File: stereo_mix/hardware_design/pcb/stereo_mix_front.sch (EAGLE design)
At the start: 31 parts, among them U1 THONKICONNOLD, U10 THONKICONNOLD, U11 THONKICONNOLD, U12 THONKICONNOLD, U13 THONKICONNOLD, U14 THONKICONNOLD, U15 THONKICONNOLD, U16 THONKICONNOLD, U17 THONKICONNOLD, U18 THONKICONNOLD, U19 THONKICONNOLD, U2 THONKICONNOLD, U20 THONKICONNOLD, U3 THONKICONNOLD, U4 THONKICONNOLD, U5 THONKICONNOLD, U6 THONKICONNOLD, U7 THONKICONNOLD, U8 THONKICONNOLD, U9 THONKICONNOLD

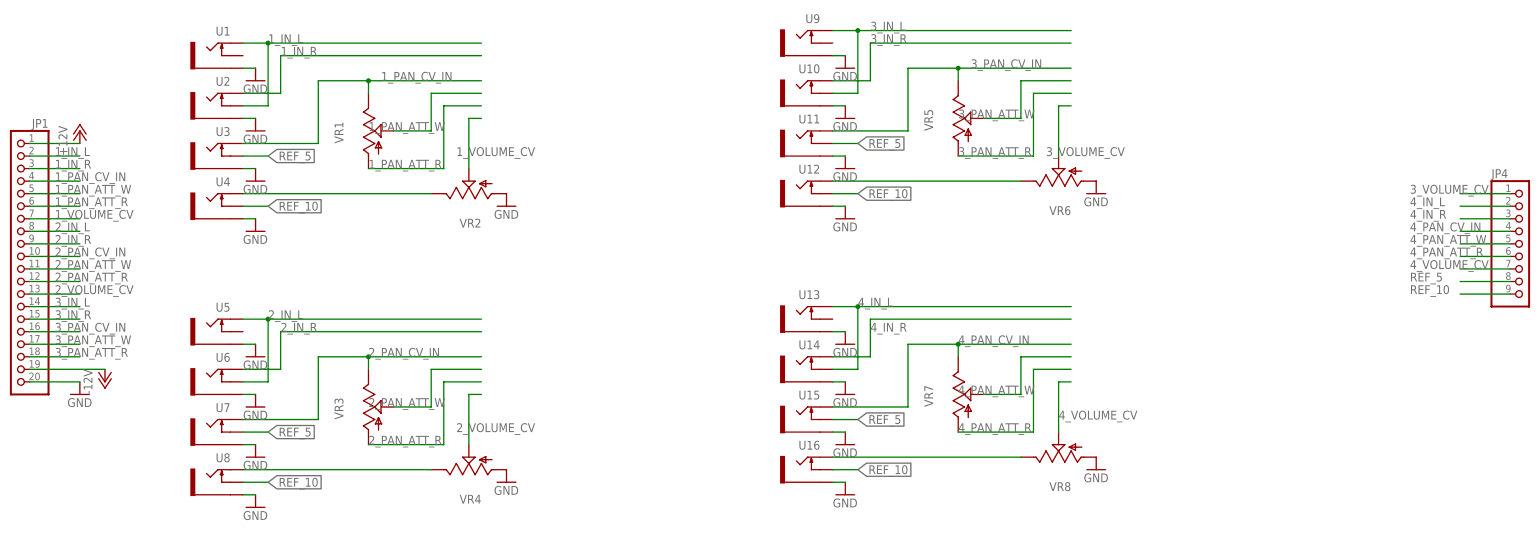
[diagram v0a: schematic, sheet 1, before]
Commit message: Add new version of stereo_mix_front panel
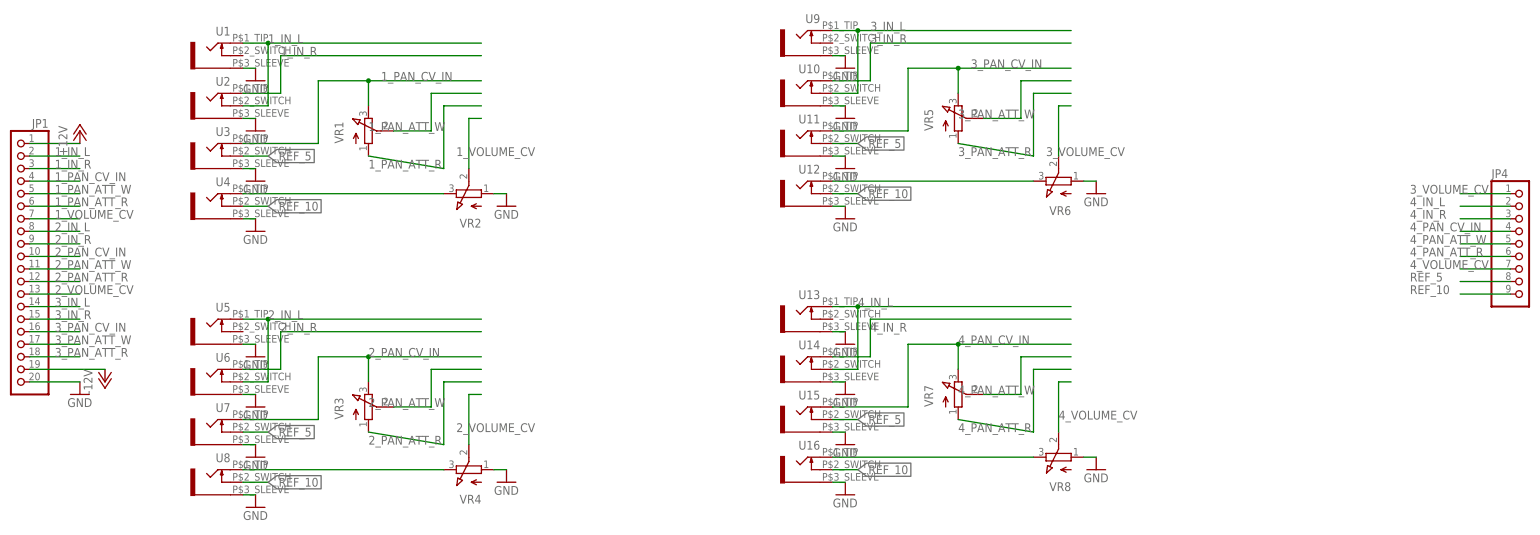
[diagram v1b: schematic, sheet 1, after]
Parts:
- removed U17, U18: THONKICONNOLD, MusicThingModular:THONKICONNOLD
- U1, U10, U11, U12, U13, U14, U15, U16, U19, U2, U20, U3, U4, U5, U6, U7, U8, U9: value THONKICONNOLD -> WQP-PJ301M-12_JACK; device MusicThingModular:THONKICONNOLD -> jhbruhn-physical:WQP-PJ301M-12_JACK
- VR1, VR2, VR3, VR4, VR5, VR6, VR7, VR8: device MusicThingModular:9MM_SNAP-IN_POT_ -> jhbruhn-physical:9MM_SNAP-IN_POT_
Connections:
- removed net BYPASS_L: JP2.3, U17.TIP
- removed net BYPASS_R: JP2.4, U18.TIP
- net 1_IN_L: now also U1.2, U2.3; no longer U1.TIP, U2.SWITCH
- net 1_IN_R: now also U2.2; no longer U2.TIP
- net 1_PAN_CV_IN: now also U3.2; no longer U3.TIP
- net 2_IN_L: now also U5.2, U6.3; no longer U5.TIP, U6.SWITCH
- net 2_IN_R: now also U6.2; no longer U6.TIP
- net 2_PAN_CV_IN: now also U7.2; no longer U7.TIP
- net 3_IN_L: now also U10.3, U9.2; no longer U10.SWITCH, U9.TIP
- net 3_IN_R: now also U10.2; no longer U10.TIP
- net 3_PAN_CV_IN: now also U11.2; no longer U11.TIP
- net 4_IN_L: now also U13.2, U14.3; no longer U13.TIP, U14.SWITCH
- net 4_IN_R: now also U14.2; no longer U14.TIP
- net 4_PAN_CV_IN: now also U15.2; no longer U15.TIP
- net GND: now also U1.1, U10.1, U11.1, U12.1, U13.1, U14.1, U15.1, U16.1, U19.1, U2.1, U20.1, U3.1, U4.1, U5.1, U6.1, U7.1, U8.1, U9.1; no longer U1.SLEEVE, U10.SLEEVE, U11.SLEEVE, U12.SLEEVE, U13.SLEEVE, U14.SLEEVE, U15.SLEEVE, U16.SLEEVE, U17.SLEEVE, U18.SLEEVE, U19.SLEEVE, U2.SLEEVE, U20.SLEEVE, U3.SLEEVE, U4.SLEEVE, U5.SLEEVE, U6.SLEEVE, U7.SLEEVE, U8.SLEEVE, U9.SLEEVE
- net N$13: now also U8.2; no longer U8.TIP
- net N$17: now also U4.2; no longer U4.TIP
- net N$21: now also U12.2; no longer U12.TIP
- net N$28: now also U16.2; no longer U16.TIP
- net OUT_L: now also JP2.3, U19.2; no longer U17.SWITCH, U19.TIP
- net OUT_R: now also JP2.4, U20.2; no longer U18.SWITCH, U20.TIP
- net REF_10: now also U12.3, U16.3, U4.3, U8.3; no longer U12.SWITCH, U16.SWITCH, U4.SWITCH, U8.SWITCH
- net REF_5: now also U11.3, U15.3, U3.3, U7.3; no longer U11.SWITCH, U15.SWITCH, U3.SWITCH, U7.SWITCH
